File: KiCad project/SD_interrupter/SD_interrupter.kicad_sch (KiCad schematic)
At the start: 36 parts, among them J1 Micro_SD_Card_Det, J2 AVR-ISP-6, J3 DIN-5, SW1 BL_SW, SW2 MAIN_SW, SW3 UP_SW, SW4 DN_SW, SW5 OK_SW, U1 LM7805_TO220, U2 4050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

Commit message: Better PCB routing
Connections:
- net CLK: now also U2.3; no longer U2.5
- net DI: now also U2.5; no longer U2.3
- net at U2.4: now also J1.3 (CMD); no longer J1.5 (CLK)
- net at U2.2: now also J1.5 (CLK); no longer J1.3 (CMD)
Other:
- moved on the sheet: U2A, U2B
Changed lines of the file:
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@@
+    (stroke (width 0) (type default) (color 0 0 0 0))
+  )
+  (wire (pts (xy 115.57 57.15) (xy 120.65 57.15))
     (stroke (width 0) (type default) (color 0 0 0 0))
   )
@@
     (stroke (width 0) (type default) (color 0 0 0 0))
   )
-  (wire (pts (xy 115.57 57.15) (xy 120.65 57.15))
-    (stroke (width 0) (type default) (color 0 0 0 0))
-  )
   (wire (pts (xy 69.85 165.1) (xy 69.85 167.64))
     (stroke (width 0) (type default) (color 0 0 0 0))
@@
     (stroke (width 0) (type default) (color 0 0 0 0))
   )
+  (wire (pts (xy 95.25 57.15) (xy 100.33 57.15))
+    (stroke (width 0) (type default) (color 0 0 0 0))
+  )
   (wire (pts (xy 201.93 57.15) (xy 201.93 54.61))
     (stroke (width 0) (type default) (color 0 0 0 0))
@@
     (stroke (width 0) (type default) (color 0 0 0 0))
   )
+  (wire (pts (xy 33.02 24.13) (xy 33.02 26.67))
+    (stroke (width 0) (type default) (color 0 0 0 0))
+  )
+  (wire (pts (xy 69.85 152.4) (xy 69.85 157.48))
+    (stroke (width 0) (type default) (color 0 0 0 0))
+  )
+  (wire (pts (xy 140.97 95.25) (xy 142.24 95.25))
+    (stroke (width 0) (type default) (color 0 0 0 0))
+  )
+  (wire (pts (xy 148.59 167.64) (xy 148.59 170.18))
+    (stroke (width 0) (type default) (color 0 0 0 0))
+  )
+  (wire (pts (xy 109.22 123.19) (xy 106.68 123.19))
+    (stroke (width 0) (type default) (color 0 0 0 0))
+  )
+  (wire (pts (xy 154.94 167.64) (xy 154.94 170.18))
+    (stroke (width 0) (type default) (color 0 0 0 0))
+  )
+  (wire (pts (xy 128.27 50.8) (xy 129.54 50.8))
+    (stroke (width 0) (type default) (color 0 0 0 0))
+  )
+  (wire (pts (xy 257.81 85.09) (xy 259.08 85.09))
+    (stroke (width 0) (type default) (color 0 0 0 0))
+  )
+  (wire (pts (xy 172.72 66.04) (xy 175.26 66.04))
+    (stroke (width 0) (type default) (color 0 0 0 0))
+  )
+  (wire (pts (xy 195.58 140.97) (xy 196.85 140.97))
+    (stroke (width 0) (type default) (color 0 0 0 0))
+  )
+  (wire (pts (xy 95.25 48.26) (xy 100.33 48.26))
+    (stroke (width 0) (type default) (color 0 0 0 0))
+  )
+  (wire (pts (xy 195.58 138.43) (xy 196.85 138.43))
+    (stroke (width 0) (type default) (color 0 0 0 0))
+  )
+  (wire (pts (xy 265.43 78.74) (xy 265.43 80.01))
+    (stroke (width 0) (type default) (color 0 0 0 0))
+  )
+  (wire (pts (xy 31.75 48.26) (xy 31.75 50.8))
+    (stroke (width 0) (type default) (color 0 0 0 0))
+  )
+  (wire (pts (xy 95.25 152.4) (xy 95.25 157.48))
+    (stroke (width 0) (type default) (color 0 0 0 0))
+  )
+  (wire (pts (xy 41.91 114.3) (xy 43.18 114.3))
+    (stroke (width 0) (type default) (color 0 0 0 0))
+  )
+  (wire (pts (xy 214.63 54.61) (xy 217.17 54.61))
+    (stroke (width 0) (type default) (color 0 0 0 0))
+  )
+  (wire (pts (xy 166.37 83.82) (xy 166.37 85.09))
+    (stroke (width 0) (type default) (color 0 0 0 0))
+  )
+  (wire (pts (xy 200.66 88.9) (xy 200.66 97.79))
+    (stroke (width 0) (type default) (color 0 0 0 0))
+  )
+  (wire (pts (xy 154.94 149.86) (xy 148.59 149.86))
+    (stroke (width 0) (type default) (color 0 0 0 0))
+  )
+  (wire (pts (xy 115.57 39.37) (xy 120.65 39.37))
+    (stroke (width 0) (type default) (color 0 0 0 0))
+  )
+  (wire (pts (xy 162.56 102.87) (xy 163.83 102.87))
+    (stroke (width 0) (type default) (color 0 0 0 0))
+  )
+  (wire (pts (xy 64.77 152.4) (xy 69.85 152.4))
+    (stroke (width 0) (type default) (color 0 0 0 0))
+  )
+  (wire (pts (xy 261.62 138.43) (xy 261.62 132.08))
+    (stroke (width 0) (type default) (color 0 0 0 0))
+  )
   (wire (pts (xy 115.57 48.26) (xy 129.54 48.26))
     (stroke (width 0) (type default) (color 0 0 0 0))
   )
-  (wire (pts (xy 33.02 24.13) (xy 33.02 26.67))
-    (stroke (width 0) (type default) (color 0 0 0 0))
-  )
-  (wire (pts (xy 69.85 152.4) (xy 69.85 157.48))
-    (stroke (width 0) (type default) (color 0 0 0 0))
-  )
-  (wire (pts (xy 140.97 95.25) (xy 142.24 95.25))
-    (stroke (width 0) (type default) (color 0 0 0 0))
-  )
-  (wire (pts (xy 148.59 167.64) (xy 148.59 170.18))
-    (stroke (width 0) (type default) (color 0 0 0 0))
-  )
-  (wire (pts (xy 109.22 123.19) (xy 106.68 123.19))
-    (stroke (width 0) (type default) (color 0 0 0 0))
-  )
-  (wire (pts (xy 154.94 167.64) (xy 154.94 170.18))
-    (stroke (width 0) (type default) (color 0 0 0 0))
-  )
-  (wire (pts (xy 128.27 50.8) (xy 129.54 50.8))
-    (stroke (width 0) (type default) (color 0 0 0 0))
-  )
-  (wire (pts (xy 257.81 85.09) (xy 259.08 85.09))
-    (stroke (width 0) (type default) (color 0 0 0 0))
-  )
-  (wire (pts (xy 172.72 66.04) (xy 175.26 66.04))
-    (stroke (width 0) (type default) (color 0 0 0 0))
-  )
-  (wire (pts (xy 195.58 140.97) (xy 196.85 140.97))
-    (stroke (width 0) (type default) (color 0 0 0 0))
-  )
-  (wire (pts (xy 195.58 138.43) (xy 196.85 138.43))
-    (stroke (width 0) (type default) (color 0 0 0 0))
-  )
-  (wire (pts (xy 265.43 78.74) (xy 265.43 80.01))
-    (stroke (width 0) (type default) (color 0 0 0 0))
-  )
-  (wire (pts (xy 31.75 48.26) (xy 31.75 50.8))
-    (stroke (width 0) (type default) (color 0 0 0 0))
-  )
-  (wire (pts (xy 95.25 152.4) (xy 95.25 157.48))
-    (stroke (width 0) (type default) (color 0 0 0 0))
-  )
-  (wire (pts (xy 41.91 114.3) (xy 43.18 114.3))
-    (stroke (width 0) (type default) (color 0 0 0 0))
-  )
-  (wire (pts (xy 214.63 54.61) (xy 217.17 54.61))
-    (stroke (width 0) (type default) (color 0 0 0 0))
-  )
-  (wire (pts (xy 166.37 83.82) (xy 166.37 85.09))
-    (stroke (width 0) (type default) (color 0 0 0 0))
-  )
-  (wire (pts (xy 95.25 48.26) (xy 100.33 48.26))
-    (stroke (width 0) (type default) (color 0 0 0 0))
-  )
-  (wire (pts (xy 200.66 88.9) (xy 200.66 97.79))
-    (stroke (width 0) (type default) (color 0 0 0 0))
-  )
-  (wire (pts (xy 154.94 149.86) (xy 148.59 149.86))
-    (stroke (width 0) (type default) (color 0 0 0 0))
-  )
-  (wire (pts (xy 115.57 39.37) (xy 120.65 39.37))
-    (stroke (width 0) (type default) (color 0 0 0 0))
-  )
-  (wire (pts (xy 162.56 102.87) (xy 163.83 102.87))
-    (stroke (width 0) (type default) (color 0 0 0 0))
-  )
-  (wire (pts (xy 64.77 152.4) (xy 69.85 152.4))
-    (stroke (width 0) (type default) (color 0 0 0 0))
-  )
-  (wire (pts (xy 261.62 138.43) (xy 261.62 132.08))
-    (stroke (width 0) (type default) (color 0 0 0 0))
-  )
   (wire (pts (xy 200.66 97.79) (xy 201.93 97.79))
     (stroke (width 0) (type default) (color 0 0 0 0))
@@
   )
   (wire (pts (xy 257.81 41.91) (xy 259.08 41.91))
-    (stroke (width 0) (type default) (color 0 0 0 0))
-  )
-  (wire (pts (xy 95.25 57.15) (xy 100.33 57.15))
     (stroke (width 0) (type default) (color 0 0 0 0))
   )
@@
     (pin "1")
   )
-  (symbol (lib_id "4xxx:4050") (at 107.95 57.15 0) (unit 2)
-    (in_bom yes) (on_board yes)
-    (property "Reference" "U2" (id 0) (at 116.84 52.07 0))
-    (property "Value" "4050" (id 1) (at 116.84 54.61 0))
-    (property "Footprint" "Package_DIP:DIP-16_W7.62mm" (id 2) (at 107.95 57.15 0)
-      (effects (font (size 1.27 1.27)) hide)
-    )
-    (property "Datasheet" "http://www.intersil.com/content/dam/intersil/documents/cd40/cd4050bms.pdf" (id 3) (at 107.95 57.15 0)
+  (symbol (lib_id "4xxx:4050") (at 107.95 48.26 0) (unit 2)
+    (in_bom yes) (on_board yes)
+    (property "Reference" "U2" (id 0) (at 116.84 43.18 0))
+    (property "Value" "4050" (id 1) (at 116.84 45.72 0))
+    (property "Footprint" "Package_DIP:DIP-16_W7.62mm" (id 2) (at 107.95 48.26 0)
+      (effects (font (size 1.27 1.27)) hide)
+    )
+    (property "Datasheet" "http://www.intersil.com/content/dam/intersil/documents/cd40/cd4050bms.pdf" (id 3) (at 107.95 48.26 0)
       (effects (font (size 1.27 1.27)) hide)
     )
@@
     (pin "1")
   )
-  (symbol (lib_id "4xxx:4050") (at 107.95 48.26 0) (unit 1)
-    (in_bom yes) (on_board yes)
-    (property "Reference" "U2" (id 0) (at 116.84 43.18 0))
-    (property "Value" "4050" (id 1) (at 116.84 45.72 0))
-    (property "Footprint" "Package_DIP:DIP-16_W7.62mm" (id 2) (at 107.95 48.26 0)
-      (effects (font (size 1.27 1.27)) hide)
-    )
-    (property "Datasheet" "http://www.intersil.com/content/dam/intersil/documents/cd40/cd4050bms.pdf" (id 3) (at 107.95 48.26 0)
-      (effects (font (size 1.27 1.27)) hide)
-    )
+  (symbol (lib_id "4xxx:4050") (at 107.95 57.15 0) (unit 1)
+    (in_bom yes) (on_board yes)
+    (property "Reference" "U2" (id 0) (at 116.84 52.07 0))
+    (property "Value" "4050" (id 1) (at 116.84 54.61 0))
+    (property "Footprint" "Package_DIP:DIP-16_W7.62mm" (id 2) (at 107.95 57.15 0)
+      (effects (font (size 1.27 1.27)) hide)
+    )
+    (property "Datasheet" "http://www.intersil.com/content/dam/intersil/documents/cd40/cd4050bms.pdf" (id 3) (at 107.95 57.15 0)
+      (effects (font (size 1.27 1.27)) hide)
+    )

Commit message: minor changes
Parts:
- added J4: Jack-DC, Connector_BarrelJack:BarrelJack_Horizontal, symbol Connector:Jack-DC
- added J5: VCC, symbol Connector:Conn_01x02_Female
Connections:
- net GND: now also J4.2, J5.2 (Pin_2)
- net VCC: now also J4.1, J5.1 (Pin_1)
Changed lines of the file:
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@@
   (junction (at 265.43 140.97) (diameter 0) (color 0 0 0 0)
   )
+  (junction (at 58.42 85.09) (diameter 0) (color 0 0 0 0)
+  )
   (junction (at 237.49 138.43) (diameter 0) (color 0 0 0 0)
   )
@@
   )
   (junction (at 123.19 152.4) (diameter 0) (color 0 0 0 0)
+  )
+  (junction (at 58.42 90.17) (diameter 0) (color 0 0 0 0)
   )
   (junction (at 109.22 110.49) (diameter 0) (color 0 0 0 0)
@@
     (stroke (width 0) (type default) (color 0 0 0 0))
   )
+  (wire (pts (xy 62.23 86.36) (xy 62.23 85.09))
+    (stroke (width 0) (type default) (color 0 0 0 0))
+  )
   (wire (pts (xy 257.81 44.45) (xy 259.08 44.45))
     (stroke (width 0) (type default) (color 0 0 0 0))
@@
     (stroke (width 0) (type default) (color 0 0 0 0))
   )
+  (wire (pts (xy 58.42 85.09) (xy 58.42 83.82))
+    (stroke (width 0) (type default) (color 0 0 0 0))
+  )
   (wire (pts (xy 71.12 100.33) (xy 71.12 101.6))
     (stroke (width 0) (type default) (color 0 0 0 0))
@@
     (stroke (width 0) (type default) (color 0 0 0 0))
   )
+  (wire (pts (xy 62.23 88.9) (xy 62.23 90.17))
+    (stroke (width 0) (type default) (color 0 0 0 0))
+  )
   (wire (pts (xy 120.65 39.37) (xy 120.65 45.72))
     (stroke (width 0) (type default) (color 0 0 0 0))
@@
     (stroke (width 0) (type default) (color 0 0 0 0))
   )
+  (wire (pts (xy 54.61 85.09) (xy 58.42 85.09))
+    (stroke (width 0) (type default) (color 0 0 0 0))
+  )
   (wire (pts (xy 148.59 167.64) (xy 148.59 170.18))
     (stroke (width 0) (type default) (color 0 0 0 0))
@@
     (stroke (width 0) (type default) (color 0 0 0 0))
   )
+  (wire (pts (xy 58.42 90.17) (xy 54.61 90.17))
+    (stroke (width 0) (type default) (color 0 0 0 0))
+  )
   (wire (pts (xy 128.27 50.8) (xy 129.54 50.8))
     (stroke (width 0) (type default) (color 0 0 0 0))
@@
     (stroke (width 0) (type default) (color 0 0 0 0))
   )
+  (wire (pts (xy 62.23 85.09) (xy 58.42 85.09))
+    (stroke (width 0) (type default) (color 0 0 0 0))
+  )
   (wire (pts (xy 106.68 110.49) (xy 106.68 111.76))
     (stroke (width 0) (type default) (color 0 0 0 0))
@@
     (stroke (width 0) (type default) (color 0 0 0 0))
   )
+  (wire (pts (xy 62.23 90.17) (xy 58.42 90.17))
+    (stroke (width 0) (type default) (color 0 0 0 0))
+  )
   (wire (pts (xy 166.37 92.71) (xy 166.37 95.25))
     (stroke (width 0) (type default) (color 0 0 0 0))
@@
   )
   (wire (pts (xy 106.68 110.49) (xy 109.22 110.49))
+    (stroke (width 0) (type default) (color 0 0 0 0))
+  )
+  (wire (pts (xy 58.42 91.44) (xy 58.42 90.17))
     (stroke (width 0) (type default) (color 0 0 0 0))
   )
@@
     )
     (property "Datasheet" "" (id 3) (at 53.34 26.67 0)
+      (effects (font (size 1.27 1.27)) hide)
+    )
+    (pin "1")
+  )
+  (symbol (lib_id "power:VCC") (at 58.42 83.82 0) (unit 1)
+    (in_bom yes) (on_board yes) (fields_autoplaced)
+    (property "Reference" "#PWR03" (id 0) (at 58.42 87.63 0)
+      (effects (font (size 1.27 1.27)) hide)
+    )
+    (property "Value" "VCC" (id 1) (at 58.42 78.74 0))
+    (property "Footprint" "" (id 2) (at 58.42 83.82 0)
+      (effects (font (size 1.27 1.27)) hide)
+    )
+    (property "Datasheet" "" (id 3) (at 58.42 83.82 0)
       (effects (font (size 1.27 1.27)) hide)
     )
@@
     (pin "1")
   )
+  (symbol (lib_id "power:GND") (at 58.42 91.44 0) (unit 1)
+    (in_bom yes) (on_board yes) (fields_autoplaced)
+    (property "Reference" "#PWR04" (id 0) (at 58.42 97.79 0)
+      (effects (font (size 1.27 1.27)) hide)
+    )
+    (property "Value" "GND" (id 1) (at 58.42 96.52 0))
+    (property "Footprint" "" (id 2) (at 58.42 91.44 0)
+      (effects (font (size 1.27 1.27)) hide)
+    )
+    (property "Datasheet" "" (id 3) (at 58.42 91.44 0)
+      (effects (font (size 1.27 1.27)) hide)
+    )
+    (pin "1")
+  )
   (symbol (lib_id "power:GND") (at 106.68 124.46 0) (unit 1)
     (in_bom yes) (on_board yes) (fields_autoplaced)
@@
     (pin "8")
   )
+  (symbol (lib_id "Connector:Conn_01x02_Female") (at 67.31 86.36 0) (unit 1)
+    (in_bom yes) (on_board yes) (fields_autoplaced)
+    (property "Reference" "J5" (id 0) (at 68.58 86.3599 0)
+      (effects (font (size 1.27 1.27)) (justify left))
+    )
+    (property "Value" "VCC" (id 1) (at 68.58 88.8999 0)
+      (effects (font (size 1.27 1.27)) (justify left))
+    )
+    (property "Footprint" "" (id 2) (at 67.31 86.36 0)
+      (effects (font (size 1.27 1.27)) hide)
+    )
+    (property "Datasheet" "~" (id 3) (at 67.31 86.36 0)
+      (effects (font (size 1.27 1.27)) hide)
+    )
+    (pin "1")
+    (pin "2")
+  )
   (symbol (lib_id "power:GND") (at 110.49 162.56 0) (unit 1)
     (in_bom yes) (on_board yes) (fields_autoplaced)
@@
     )
     (property "Datasheet" "~" (id 3) (at 88.9 105.41 0)
+      (effects (font (size 1.27 1.27)) hide)
+    )
+    (pin "1")
+    (pin "2")
+  )
+  (symbol (lib_id "Connector:Jack-DC") (at 46.99 87.63 0) (unit 1)
+    (in_bom yes) (on_board yes) (fields_autoplaced)
+    (property "Reference" "J4" (id 0) (at 46.99 78.74 0))
+    (property "Value" "Jack-DC" (id 1) (at 46.99 81.28 0))
+    (property "Footprint" "Connector_BarrelJack:BarrelJack_Horizontal" (id 2) (at 48.26 88.646 0)
+      (effects (font (size 1.27 1.27)) hide)
+    )
+    (property "Datasheet" "~" (id 3) (at 48.26 88.646 0)
       (effects (font (size 1.27 1.27)) hide)
     )
@@
       (reference "#PWR02") (unit 1) (value "+3.3V") (footprint "")
     )
+    (path "/2aca912f-7e47-49db-9976-cfed18257321"
+      (reference "#PWR03") (unit 1) (value "VCC") (footprint "")
+    )
+    (path "/570f147d-d2e2-4f0c-acd7-e5a9656e9667"
+      (reference "#PWR04") (unit 1) (value "GND") (footprint "")
+    )
     (path "/f5ad944c-d4c5-448f-becd-1e591c8b8925"
       (reference "#PWR0101") (unit 1) (value "GND") (footprint "")
@@
       (reference "J3") (unit 1) (value "DIN-5") (footprint "w_conn_av:din-5")
     )
+    (path "/9da991a0-64c0-4592-a5ee-acfb0ec3e8c3"
+      (reference "J4") (unit 1) (value "Jack-DC") (footprint "Connector_BarrelJack:BarrelJack_Horizontal")
+    )
+    (path "/6f4c1976-0423-4dca-bd5b-a5af17e192b2"
+      (reference "J5") (unit 1) (value "VCC") (footprint "")
+    )
     (path "/0f10510d-6ad1-4e07-b5dd-f11eb28d7d3c"

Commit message: minor changes
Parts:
- J5: footprint (none) -> Connector_PinSocket_2.54mm:PinSocket_1x02_P2.54mm_Vertical
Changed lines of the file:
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@@
       (effects (font (size 1.27 1.27)) (justify left))
     )
-    (property "Footprint" "" (id 2) (at 67.31 86.36 0)
+    (property "Footprint" "Connector_PinSocket_2.54mm:PinSocket_1x02_P2.54mm_Vertical" (id 2) (at 67.31 86.36 0)
       (effects (font (size 1.27 1.27)) hide)
     )
@@
     )
     (path "/6f4c1976-0423-4dca-bd5b-a5af17e192b2"
-      (reference "J5") (unit 1) (value "VCC") (footprint "")
+      (reference "J5") (unit 1) (value "VCC") (footprint "Connector_PinSocket_2.54mm:PinSocket_1x02_P2.54mm_Vertical")
     )
     (path "/0f10510d-6ad1-4e07-b5dd-f11eb28d7d3c"

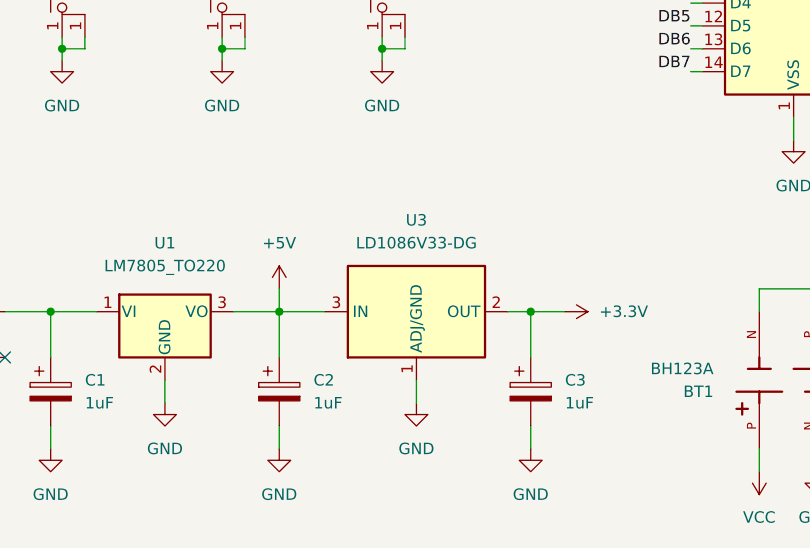
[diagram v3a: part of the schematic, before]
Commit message: different 3.3V regulator footprint
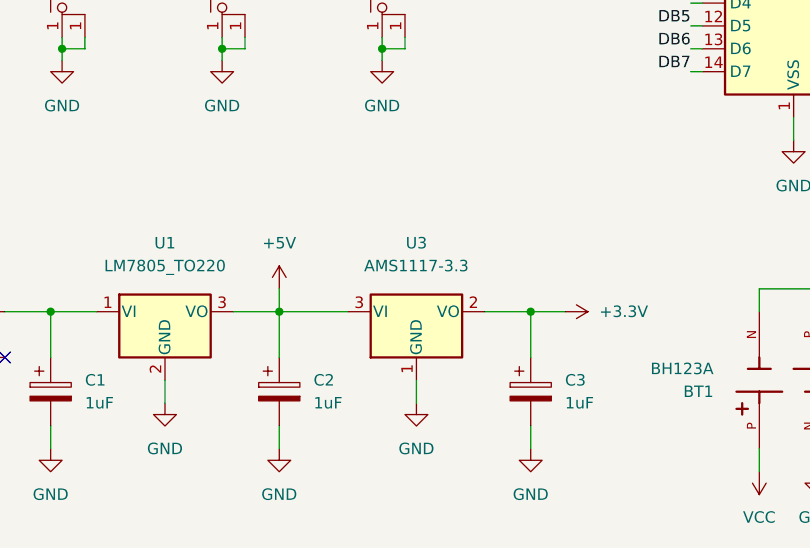
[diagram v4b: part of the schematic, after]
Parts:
- removed U3: LD1086V33-DG, Package_TO_SOT_THT:TO-92, symbol Regulator_Linear:LD1086V33-DG
- added U3: AMS1117-3.3, Package_TO_SOT_SMD:SOT-223-3_TabPin2, symbol Regulator_Linear:AMS1117-3.3
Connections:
- net +3.3V: now also U3.2 (VO)
- net +5V: now also U3.3 (VI)
- net GND: now also U3.1 (GND)
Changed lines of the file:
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@@
     (stroke (width 0) (type default) (color 0 0 0 0))
   )
-  (wire (pts (xy 95.25 152.4) (xy 100.33 152.4))
+  (wire (pts (xy 95.25 152.4) (xy 102.87 152.4))
     (stroke (width 0) (type default) (color 0 0 0 0))
   )
@@
     (stroke (width 0) (type default) (color 0 0 0 0))
   )
-  (wire (pts (xy 120.65 152.4) (xy 123.19 152.4))
+  (wire (pts (xy 118.11 152.4) (xy 123.19 152.4))
     (stroke (width 0) (type default) (color 0 0 0 0))
   )
@@
     )
     (pin "1")
-  )
-  (symbol (lib_id "Regulator_Linear:LD1086V33-DG") (at 110.49 152.4 0) (unit 1)
-    (in_bom yes) (on_board yes) (fields_autoplaced)
-    (property "Reference" "U3" (id 0) (at 110.49 142.24 0))
-    (property "Value" "LD1086V33-DG" (id 1) (at 110.49 144.78 0))
-    (property "Footprint" "Package_TO_SOT_THT:TO-92" (id 2) (at 110.49 139.7 0)
-      (effects (font (size 1.27 1.27)) hide)
-    )
-    (property "Datasheet" "https://www.st.com/resource/en/datasheet/ld1086.pdf" (id 3) (at 110.49 137.16 0)
-      (effects (font (size 1.27 1.27)) hide)
-    )
-    (pin "1")
-    (pin "2")
-    (pin "3")
   )
   (symbol (lib_id "power:GND") (at 260.35 146.05 0) (unit 1)
@@
     )
     (pin "1")
+  )
+  (symbol (lib_id "Regulator_Linear:AMS1117-3.3") (at 110.49 152.4 0) (unit 1)
+    (in_bom yes) (on_board yes) (fields_autoplaced)
+    (property "Reference" "U3" (id 0) (at 110.49 144.78 0))
+    (property "Value" "AMS1117-3.3" (id 1) (at 110.49 147.32 0))
+    (property "Footprint" "Package_TO_SOT_SMD:SOT-223-3_TabPin2" (id 2) (at 110.49 147.32 0)
+      (effects (font (size 1.27 1.27)) hide)
+    )
+    (property "Datasheet" "http://www.advanced-monolithic.com/pdf/ds1117.pdf" (id 3) (at 113.03 158.75 0)
+      (effects (font (size 1.27 1.27)) hide)
+    )
+    (pin "1")
+    (pin "2")
+    (pin "3")
   )
   (symbol (lib_id "power:GND") (at 175.26 67.31 0) (unit 1)
@@
       (reference "U2") (unit 7) (value "4050") (footprint "Package_DIP:DIP-16_W7.62mm")
     )
-    (path "/250c4b1f-7140-43e5-99f8-c84f36152dff"
-      (reference "U3") (unit 1) (value "LD1086V33-DG") (footprint "Package_TO_SOT_THT:TO-92")
+    (path "/5bbcf254-861a-41ee-89df-9643724e7f70"
+      (reference "U3") (unit 1) (value "AMS1117-3.3") (footprint "Package_TO_SOT_SMD:SOT-223-3_TabPin2")
     )
     (path "/f4cf6656-f4db-4270-b521-135c7201081c"
